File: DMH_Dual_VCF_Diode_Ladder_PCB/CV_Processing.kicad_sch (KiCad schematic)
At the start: 8 parts, among them SW4 SW_SPDT_321, SW6 SW_SPDT_321

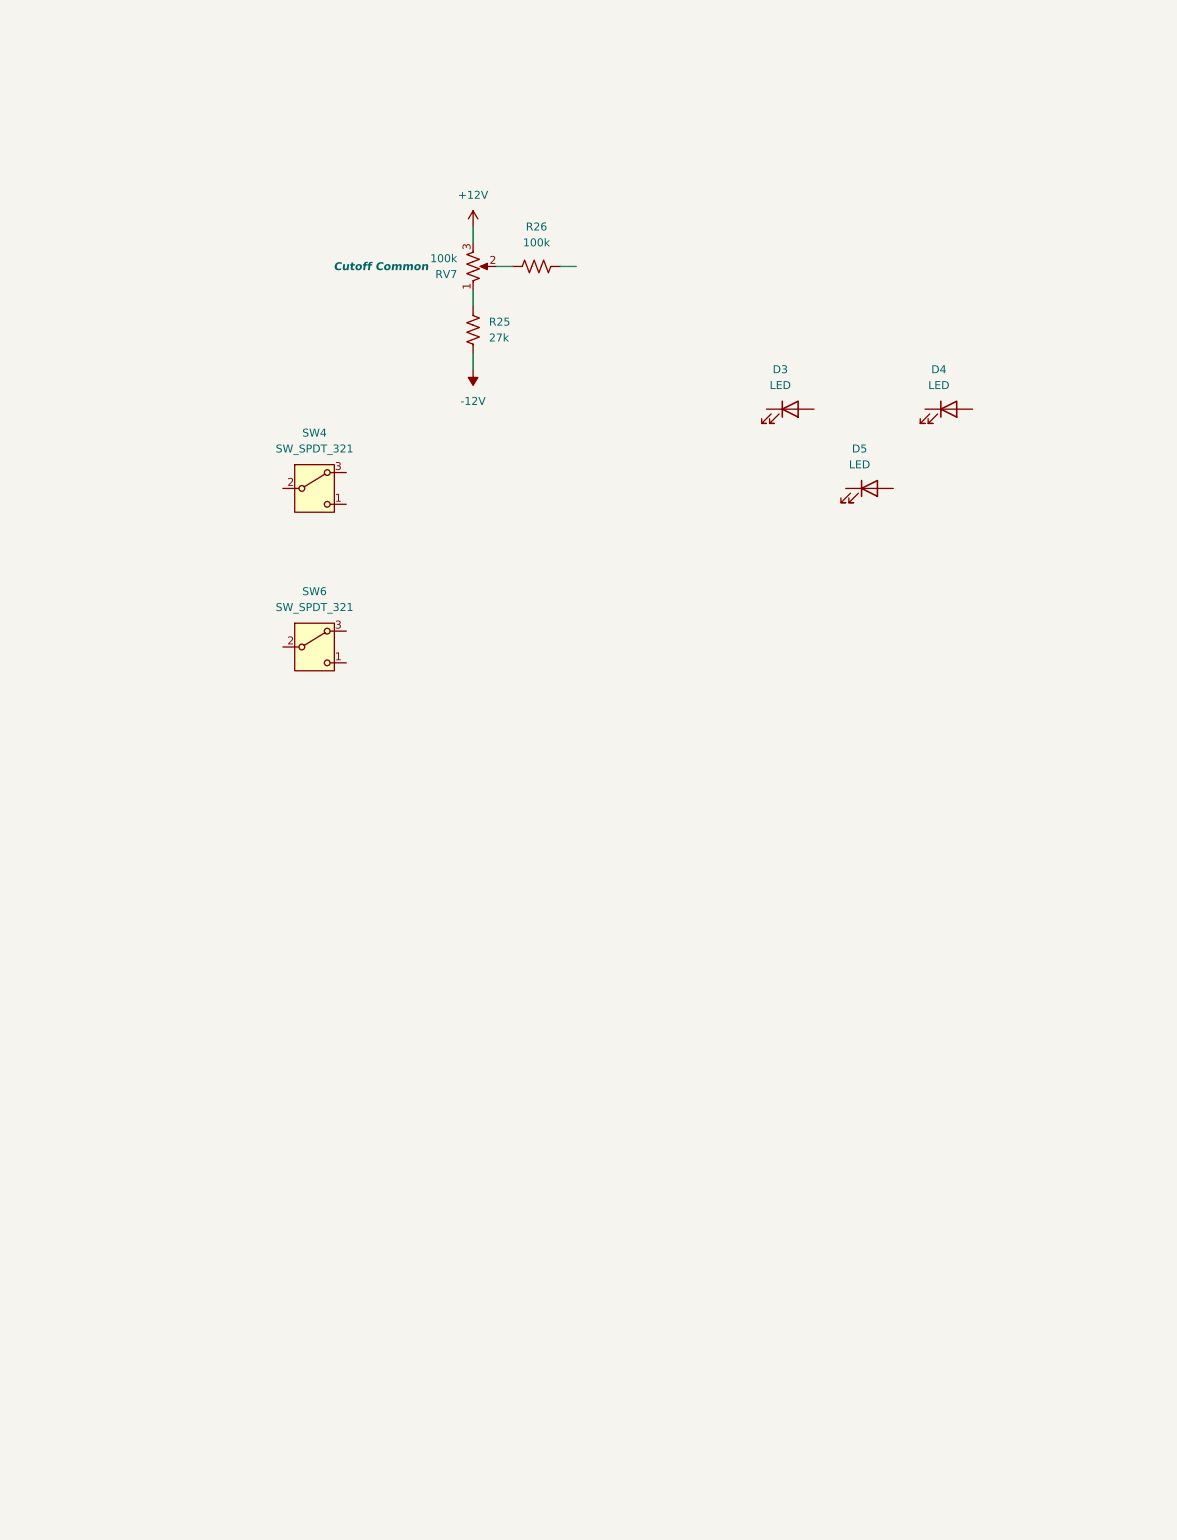
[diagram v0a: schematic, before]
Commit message: Made CV processing page
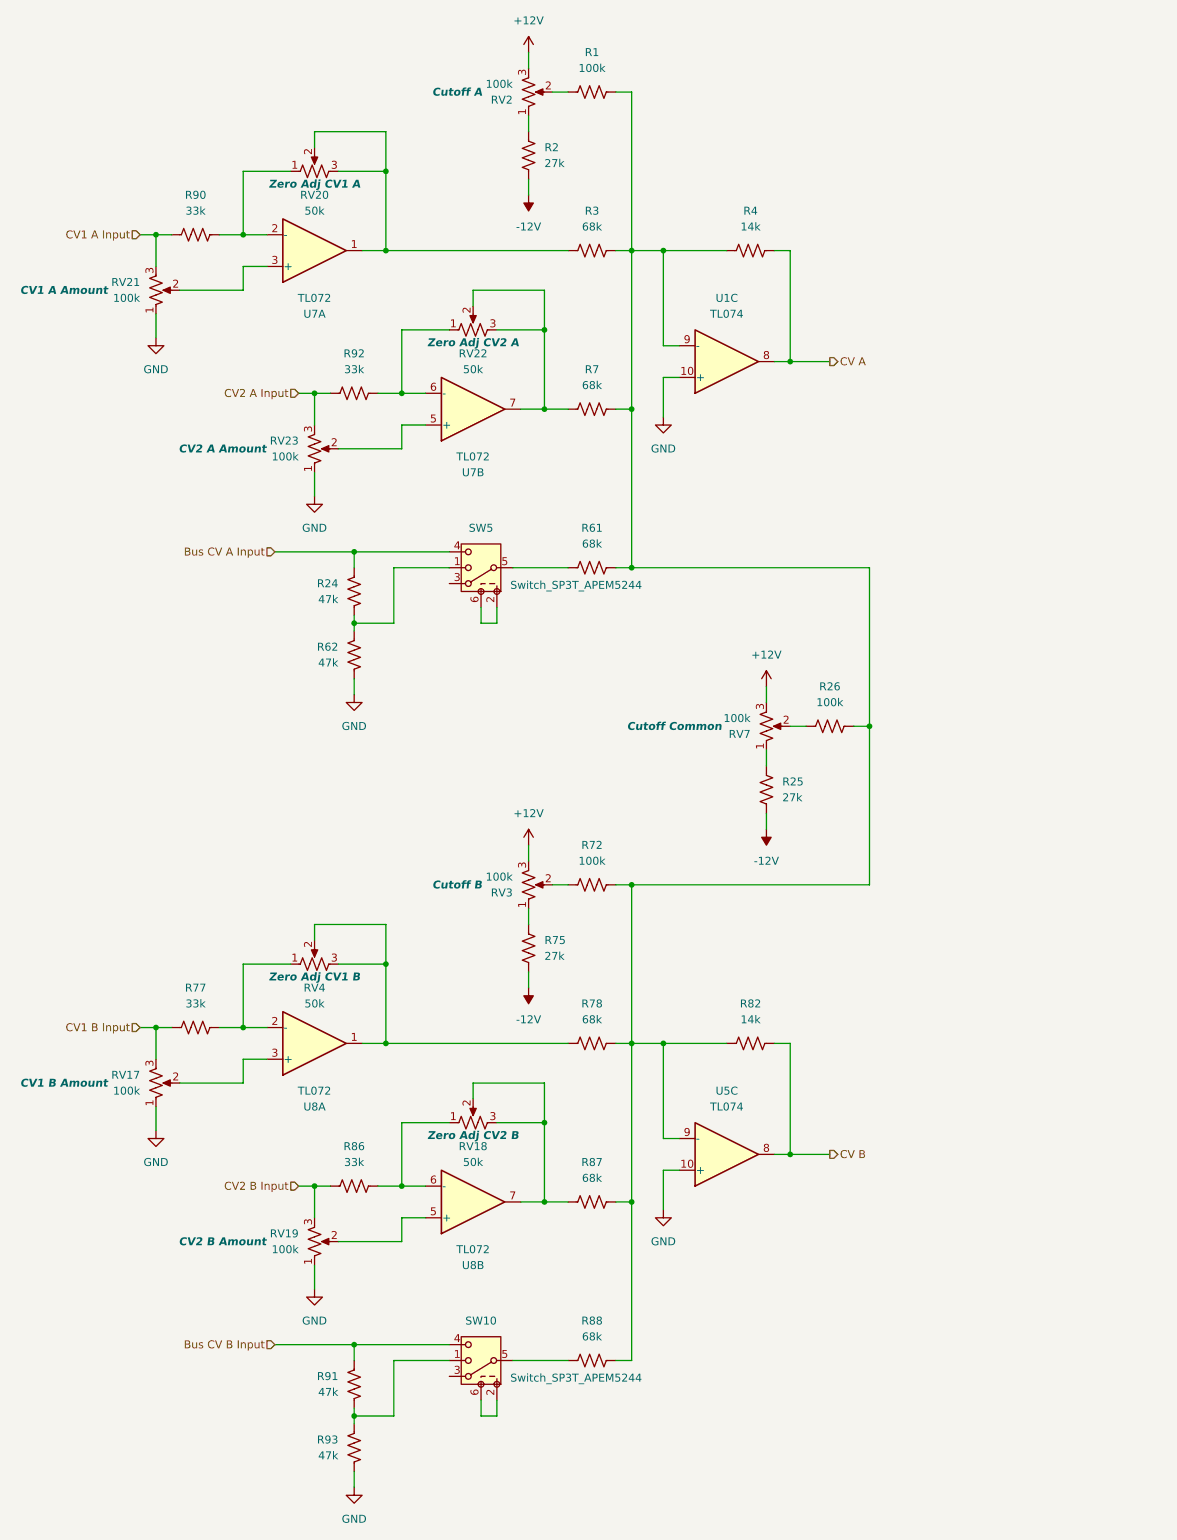
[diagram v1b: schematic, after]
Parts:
- removed D3, D4, D5: LED, LED_THT:LED_D3.0mm, symbol Device:LED
- removed SW4, SW6: SW_SPDT_321, SynthStuff:Toggle_Switch_THT, symbol Switch:SW_SPDT_321
- added R1, R72: 100k, Resistor_THT:R_Axial_DIN0207_L6.3mm_D2.5mm_P7.62mm_Horizontal, symbol Device:R_US
- added R2, R75: 27k, Resistor_THT:R_Axial_DIN0207_L6.3mm_D2.5mm_P7.62mm_Horizontal, symbol Device:R_US
- added R24, R62, R91, R93: 47k, Resistor_THT:R_Axial_DIN0207_L6.3mm_D2.5mm_P7.62mm_Horizontal, symbol Device:R_US
- added R3, R61, R7, R78, R87, R88: 68k, Resistor_THT:R_Axial_DIN0207_L6.3mm_D2.5mm_P7.62mm_Horizontal, symbol Device:R_US
- added R4, R82: 14k, Resistor_THT:R_Axial_DIN0207_L6.3mm_D2.5mm_P7.62mm_Horizontal, symbol Device:R_US
- added R77, R86, R90, R92: 33k, Resistor_THT:R_Axial_DIN0207_L6.3mm_D2.5mm_P7.62mm_Horizontal, symbol Device:R_US
- added RV17, RV19, RV21, RV23: 100k, SynthStuff:Potentiometer_TT_P110KH1, symbol Device:R_Potentiometer_US
- added RV18, RV20, RV22, RV4: 50k, Potentiometer_THT:Potentiometer_Bourns_3296W_Vertical, symbol Device:R_Potentiometer_US
- added RV2, RV3: 100k, SynthStuff:Potentiometer_Alpha_RD901F-40-00D_Single_Vertical, symbol Device:R_Potentiometer_US
- added SW10, SW5: Switch_SP3T_APEM5244, symbol SynthStuff:Switch_SP3T
- added U1, U5: TL074, Package_DIP:DIP-14_W7.62mm_Socket, symbol Amplifier_Operational:TL074
- added U7, U8: TL072, Package_DIP:DIP-8_W7.62mm_Socket, symbol Amplifier_Operational:TL072
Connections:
- net +12V: now also RV2.3, RV3.3
- net -12V: now also R2.2, R75.2
- net at R26.2: now also R1.2, R3.2, R4.1, R61.1, R7.2, R72.2, R78.2, R82.1, R87.2, R88.1, U1.9 (-), U5.9 (-)
- new net: R75.1, RV3.1
- new net: R72.1, RV3.2
- new net: R3.1, RV20.2, RV20.3, U7.1
- new net: R86.2, RV18.1, U8.6 (-)
- new net: R87.1, RV18.2, RV18.3, U8.7
- new net: R61.2, SW5.5
- new net: R92.2, RV22.1, U7.6 (-)
- new net: R2.1, RV2.1
- new net: R78.1, RV4.2, RV4.3, U8.1
- new net: R77.2, RV4.1, U8.2 (-)
- new net: RV19.2, U8.5 (+)
- new net: R90.2, RV20.1, U7.2 (-)
- new net: R24.1, R62.2, SW5.1
- new net: RV21.2, U7.3 (+)
- new net: R7.1, RV22.2, RV22.3, U7.7
- new net: R91.1, R93.2, SW10.1
- new net: SW10.2, SW10.6
- new net: R88.2, SW10.5
- new net: R1.1, RV2.2
- new net: RV23.2, U7.5 (+)
- new net: RV17.2, U8.3 (+)
- new net: SW5.2, SW5.6
- new net Bus CV A Input: R24.2, SW5.4
- new net Bus CV B Input: R91.2, SW10.4
- new net CV A: R4.2, U1.8
- new net CV B: R82.2, U5.8
- new net CV1 A Input: R90.1, RV21.3
- new net CV1 B Input: R77.1, RV17.3
- new net CV2 A Input: R92.1, RV23.3
- new net CV2 B Input: R86.1, RV19.3
- new net GND: R62.1, R93.1, RV17.1, RV19.1, RV21.1, RV23.1, U1.10 (+), U5.10 (+)
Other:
- moved on the sheet: R25, R26, RV7

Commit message: Finished designing circuit
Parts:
- added D3, D4, D5: LED, LED_THT:LED_D3.0mm, symbol Device:LED
- added R94, R95, R96: 3k3, Resistor_THT:R_Axial_DIN0207_L6.3mm_D2.5mm_P7.62mm_Horizontal, symbol Device:R_US
- added SW6: SW_DPDT, SynthStuff:PinHeader_2x03_P2.54mm_Vertical_142536, symbol SynthStuff:Switch_DPDT
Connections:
- net +12V: now also SW6.5 (B)
- net CV A: now also SW6.1 (A)
- net CV B: now also SW6.3 (C)
- net GND: now also D3.1 (K), D4.1 (K), D5.1 (K)
- new net: R94.1, R95.1, SW6.6 (C)
- new net: D3.2 (A), R94.2
- new net: D4.2 (A), R95.2
- new net: D5.2 (A), R96.2
- new net: R96.1, SW6.4 (A)
- new net Link Switch: SW6.2 (B)
- no-connect marks 0 -> 2
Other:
- moved on the sheet: R25, R26, RV7

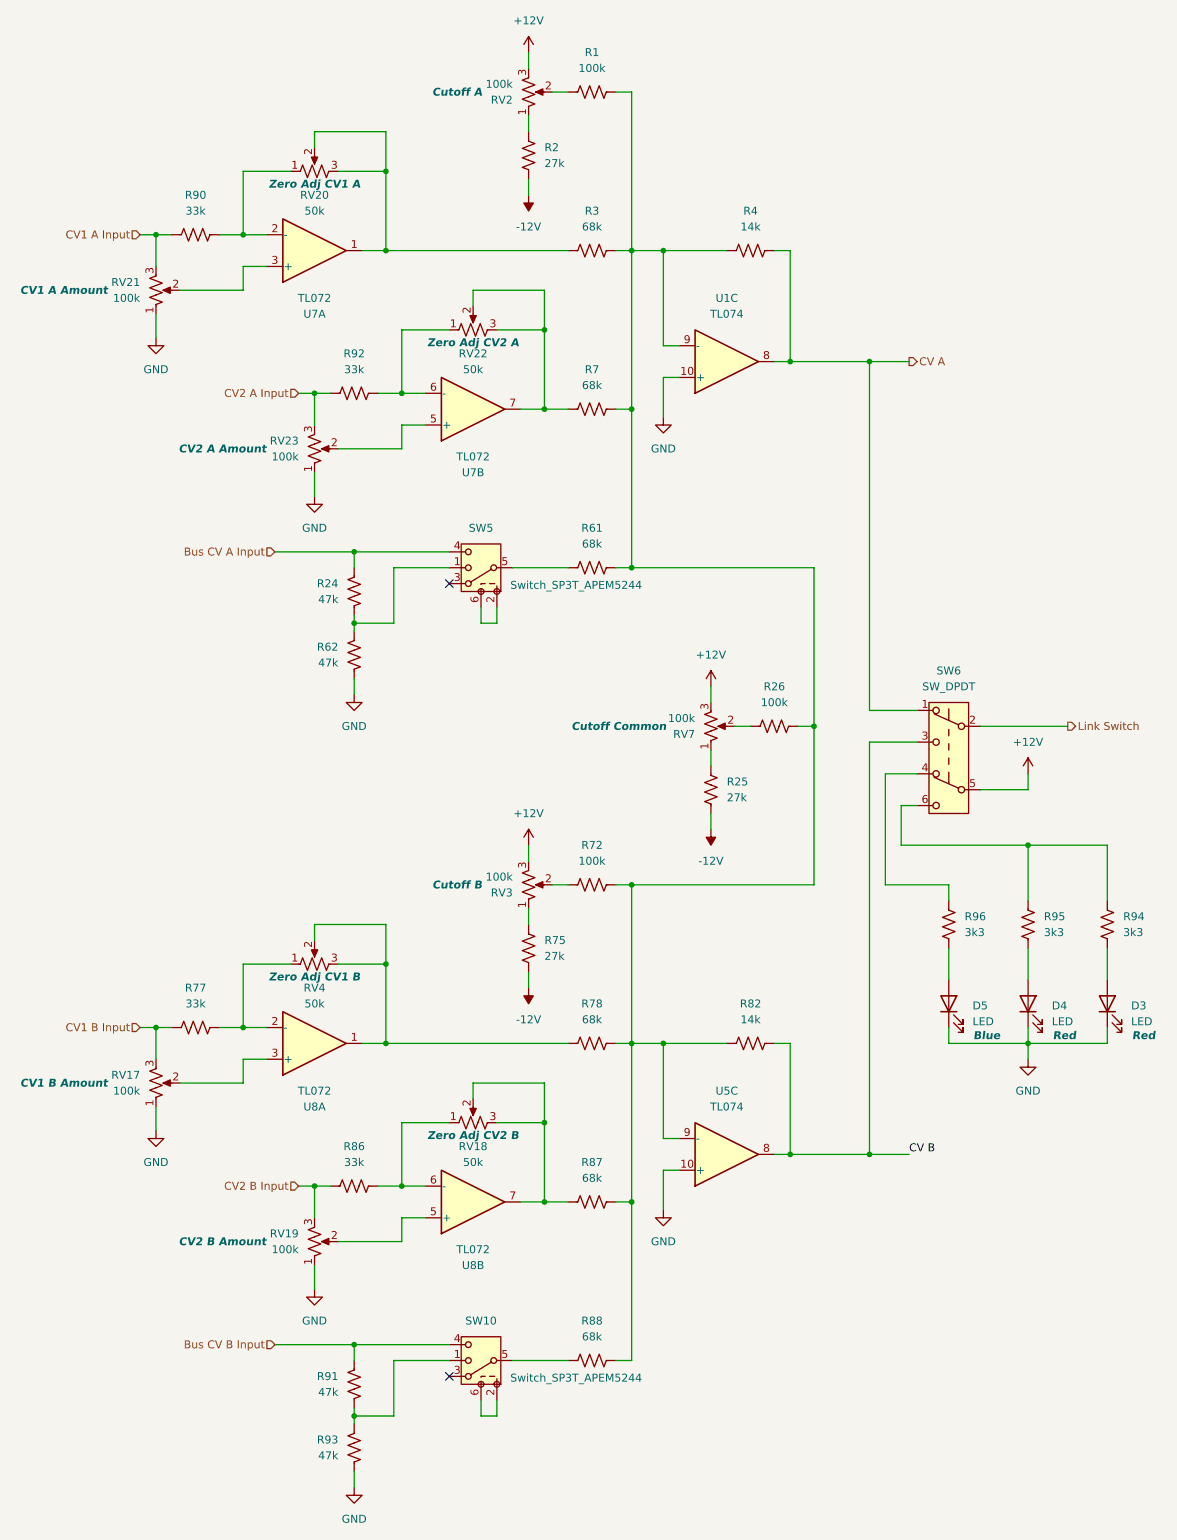
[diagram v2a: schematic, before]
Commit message: Reannotated whole schematic
OpAmp annotation is still tentative.
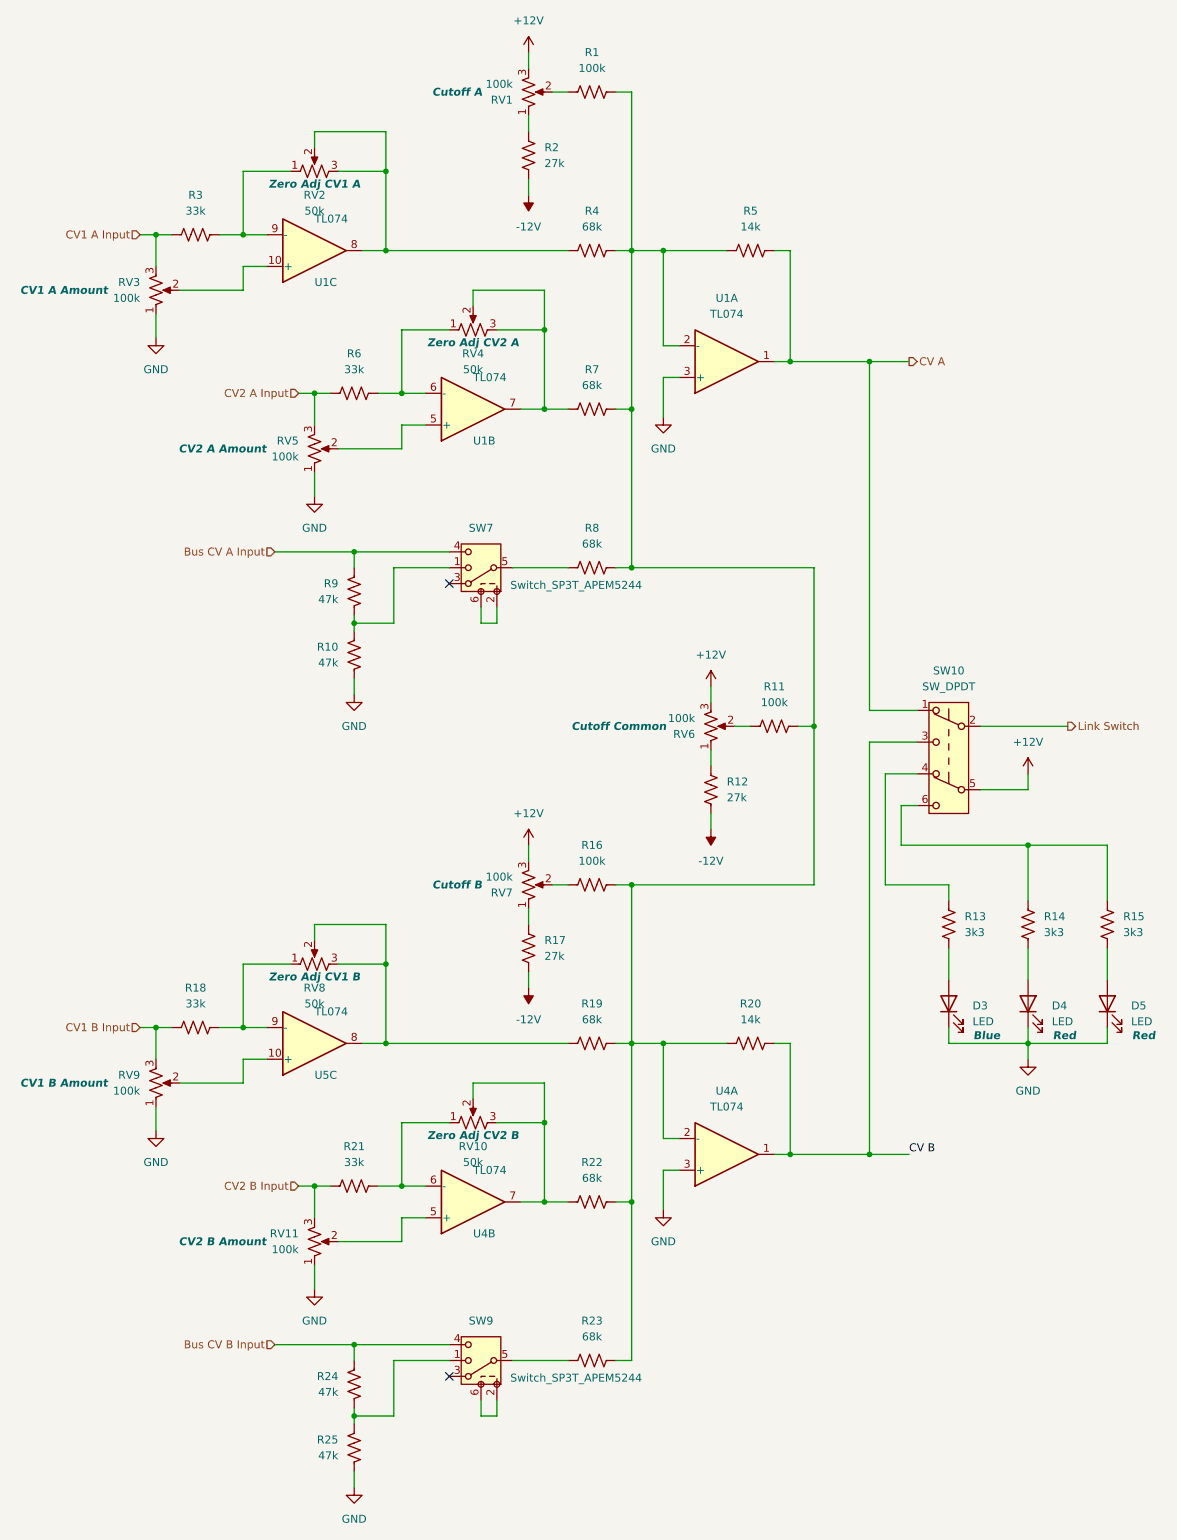
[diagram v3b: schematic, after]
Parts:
- U1: renamed from U7; value TL072 -> TL074; footprint Package_DIP:DIP-8_W7.62mm_Socket -> Package_DIP:DIP-14_W7.62mm_Socket; symbol Amplifier_Operational:TL072 -> Amplifier_Operational:TL074
- U4, U5: renamed from U8; value TL072 -> TL074; footprint Package_DIP:DIP-8_W7.62mm_Socket -> Package_DIP:DIP-14_W7.62mm_Socket; symbol Amplifier_Operational:TL072 -> Amplifier_Operational:TL074
- renumbered D5 to D3, D3 to D5, R62 to R10, R26 to R11, R25 to R12, R96 to R13, R95 to R14, R94 to R15, R72 to R16, R75 to R17, R77 to R18, R78 to R19, R82 to R20, R86 to R21, R87 to R22, R88 to R23, R91 to R24, R93 to R25, R90 to R3, R3 to R4, R4 to R5, R92 to R6, R61 to R8, R24 to R9, RV2 to RV1, RV18 to RV10, RV19 to RV11, RV20 to RV2, RV21 to RV3, RV22 to RV4, RV23 to RV5, RV7 to RV6, RV3 to RV7, RV4 to RV8, RV17 to RV9, SW6 to SW10, SW5 to SW7, SW10 to SW9, U5 to U4
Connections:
- net CV A: now also U1.1; no longer U1.8
- net CV B: now also U4.1; no longer U4.8
- net GND: now also U1.3 (+), U4.3 (+); no longer U1.10 (+), U4.10 (+)
- net at R1.2, R11.2, R16.2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: now also U1.2 (-), U4.2 (-); no longer U1.9 (-), U4.9 (-)
- net at R4.1, RV2.2, RV2.3: now also U1.8; no longer U1.1
- net at R19.1, RV8.2, RV8.3: now also U5.8; no longer U5.1
- net at R18.2, RV8.1: now also U5.9 (-); no longer U5.2 (-)
- net at R3.2, RV2.1: now also U1.9 (-); no longer U1.2 (-)
- net at RV3.2: now also U1.10 (+); no longer U1.3 (+)
- net at RV9.2: now also U5.10 (+); no longer U5.3 (+)

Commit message: Reannotated OpAmps and cleared errors
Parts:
- renumbered U4 to U2, U5 to U2
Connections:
- net CV A: now also U1.8; no longer U1.1
- net CV B: now also U2.8; no longer U2.1
- net GND: now also U1.10 (+), U2.10 (+); no longer U1.3 (+), U2.3 (+)
- net at R1.2, R11.2, R16.2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: now also U1.9 (-), U2.9 (-); no longer U1.2 (-), U2.2 (-)
- net at R4.1, RV2.2, RV2.3: now also U1.1; no longer U1.8
- net at R19.1, RV8.2, RV8.3: now also U2.1; no longer U2.8
- net at R18.2, RV8.1: now also U2.2 (-); no longer U2.9 (-)
- net at R3.2, RV2.1: now also U1.2 (-); no longer U1.9 (-)
- net at RV3.2: now also U1.3 (+); no longer U1.10 (+)
- net at RV9.2: now also U2.3 (+); no longer U2.10 (+)
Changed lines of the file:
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@@
 		(at 129.54 208.28 0)
 		(mirror x)
-		(unit 1)
+		(unit 3)
 		(exclude_from_sim no)
 		(in_bom yes)
@@
 		(dnp no)
 		(fields_autoplaced yes)
-		(property "Reference" "U4"
+		(property "Reference" "U2"
 			(at 129.54 198.12 0)
 			(effects
@@
 			(project "DMH_Dual_VCF_Diode_Ladder_PCB"
 				(path "/58f4306d-5387-4983-bb08-41a2313fd315/ec2d44bc-ed06-4f0b-a22e-df640fa5e089"
-					(reference "U4")
-					(unit 1)
+					(reference "U2")
+					(unit 3)
 				)
 			)
@@
 		(at 63.5 190.5 0)
 		(mirror x)
-		(unit 3)
-		(exclude_from_sim no)
-		(in_bom yes)
-		(on_board yes)
-		(dnp no)
-		(property "Reference" "U5"
+		(unit 1)
+		(exclude_from_sim no)
+		(in_bom yes)
+		(on_board yes)
+		(dnp no)
+		(property "Reference" "U2"
 			(at 63.5 195.58 0)
 			(effects
@@
 			(project "DMH_Dual_VCF_Diode_Ladder_PCB"
 				(path "/58f4306d-5387-4983-bb08-41a2313fd315/ec2d44bc-ed06-4f0b-a22e-df640fa5e089"
-					(reference "U5")
-					(unit 3)
+					(reference "U2")
+					(unit 1)
 				)
 			)
@@
 		(at 129.54 81.28 0)
 		(mirror x)
-		(unit 1)
+		(unit 3)
 		(exclude_from_sim no)
 		(in_bom yes)
@@
 				(path "/58f4306d-5387-4983-bb08-41a2313fd315/ec2d44bc-ed06-4f0b-a22e-df640fa5e089"
 					(reference "U1")
-					(unit 1)
+					(unit 3)
 				)
 			)
@@
 		(at 63.5 63.5 0)
 		(mirror x)
-		(unit 3)
+		(unit 1)
 		(exclude_from_sim no)
 		(in_bom yes)
@@
 				(path "/58f4306d-5387-4983-bb08-41a2313fd315/ec2d44bc-ed06-4f0b-a22e-df640fa5e089"
 					(reference "U1")
-					(unit 3)
+					(unit 1)
 				)
 			)
@@
 		(on_board yes)
 		(dnp no)
-		(property "Reference" "U4"
+		(property "Reference" "U2"
 			(at 88.9 220.98 0)
 			(effects
@@
 			(project "DMH_Dual_VCF_Diode_Ladder_PCB"
 				(path "/58f4306d-5387-4983-bb08-41a2313fd315/ec2d44bc-ed06-4f0b-a22e-df640fa5e089"
-					(reference "U4")
+					(reference "U2")
 					(unit 2)
 				)

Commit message: Updated switches symbols and fps
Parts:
- removed SW7, SW9: Switch_SP3T_APEM5244, symbol SynthStuff:Switch_SP3T
- added SW7, SW9: SW_SPDT_OnOffOn, SynthStuff:Toggle_Switch_TE, symbol Switch:SW_SPDT
- SW10: value SW_DPDT -> SW_DPDT_OnOn; footprint SynthStuff:PinHeader_2x03_P2.54mm_Vertical_142536 -> SynthStuff:Toggle_Switch_2_Poles_TE
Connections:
- net Bus CV A Input: now also SW7.3 (C)
- net Bus CV B Input: now also SW9.3 (C)
- net at R8.2: now also SW7.2 (B)
- net at R10.2, R9.1: now also SW7.1 (A)
- net at R24.1, R25.2: now also SW9.1 (A)
- net at R23.2: now also SW9.2 (B)
- no-connect marks 2 -> 0
